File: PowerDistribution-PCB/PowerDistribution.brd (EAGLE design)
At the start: 166 x 53.5 mm, 47 parts, among them IC1 MAX3041CUE, IC2 MAX3041CUE, IC3 MAX3041CUE, IC4 MAX3041CUE, IC9 SN75176ASOIC

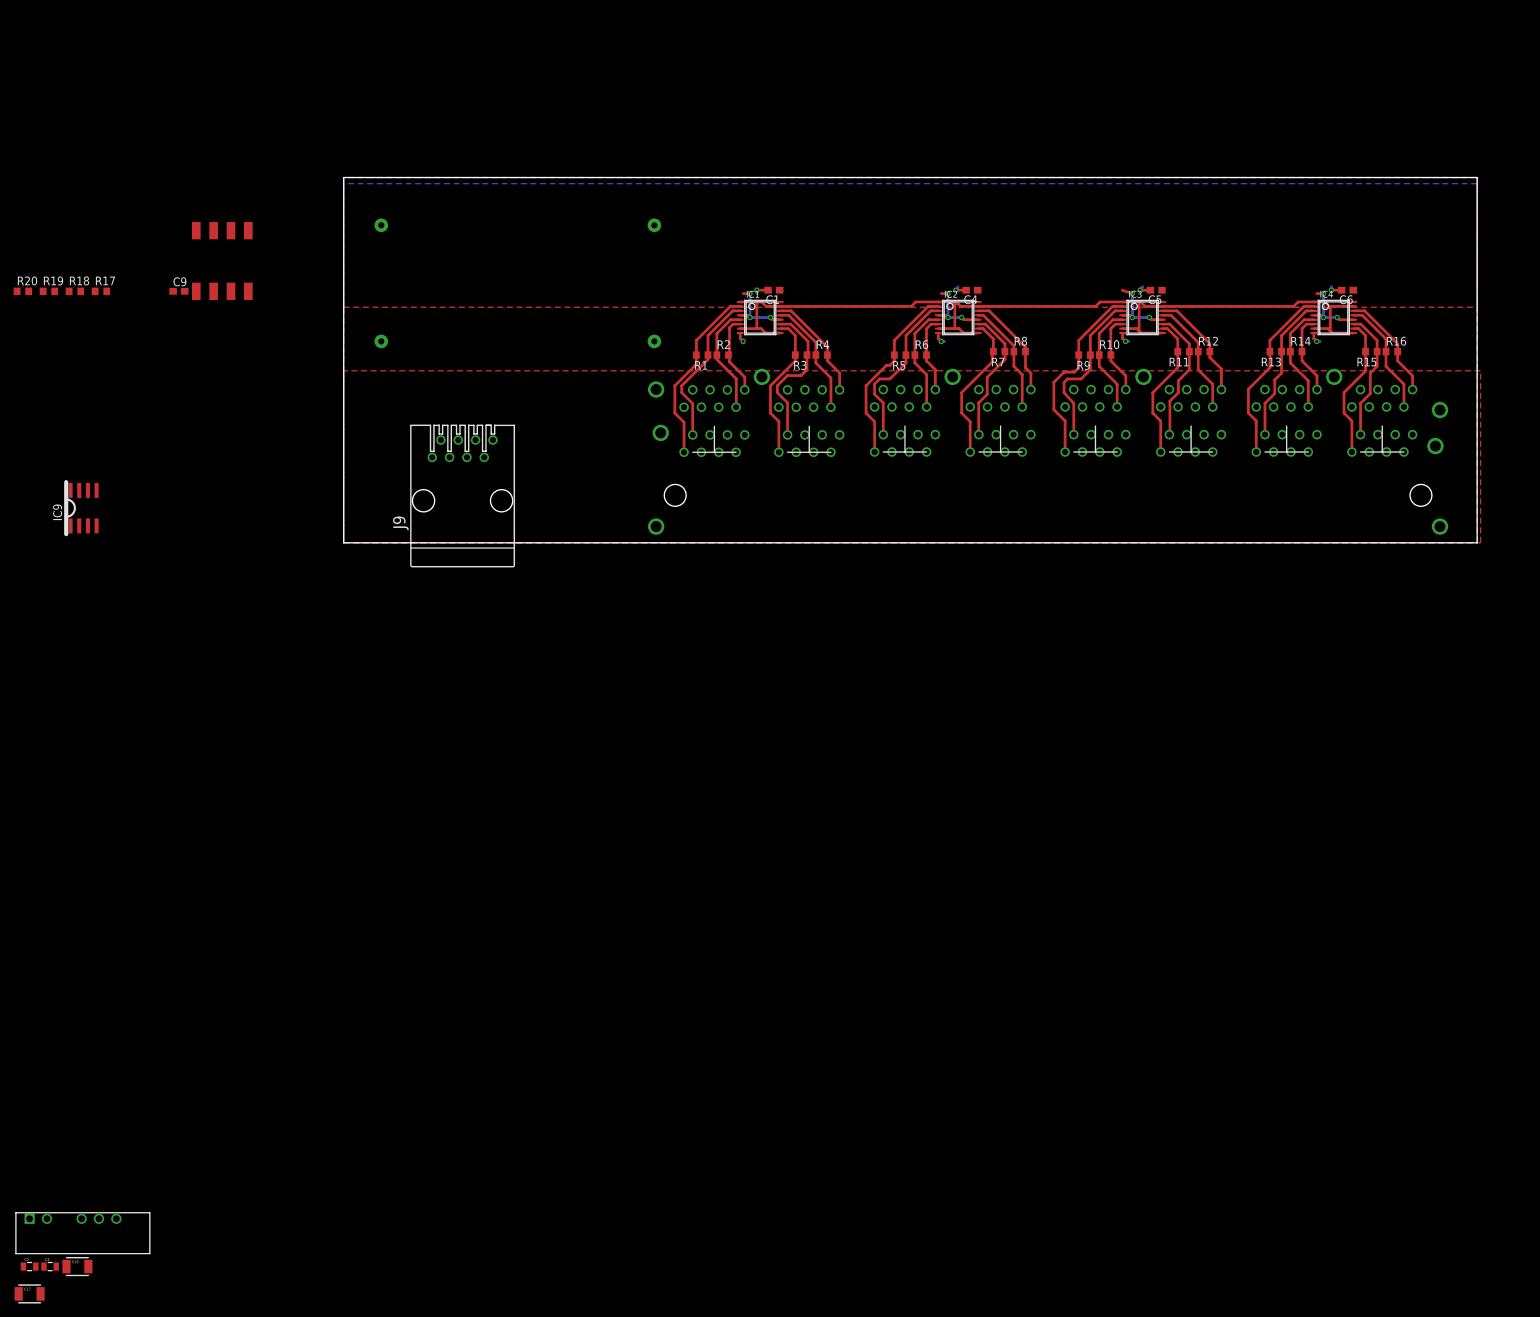
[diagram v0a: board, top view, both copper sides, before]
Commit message: Finish routing power distribution PCB; still need to fit to case
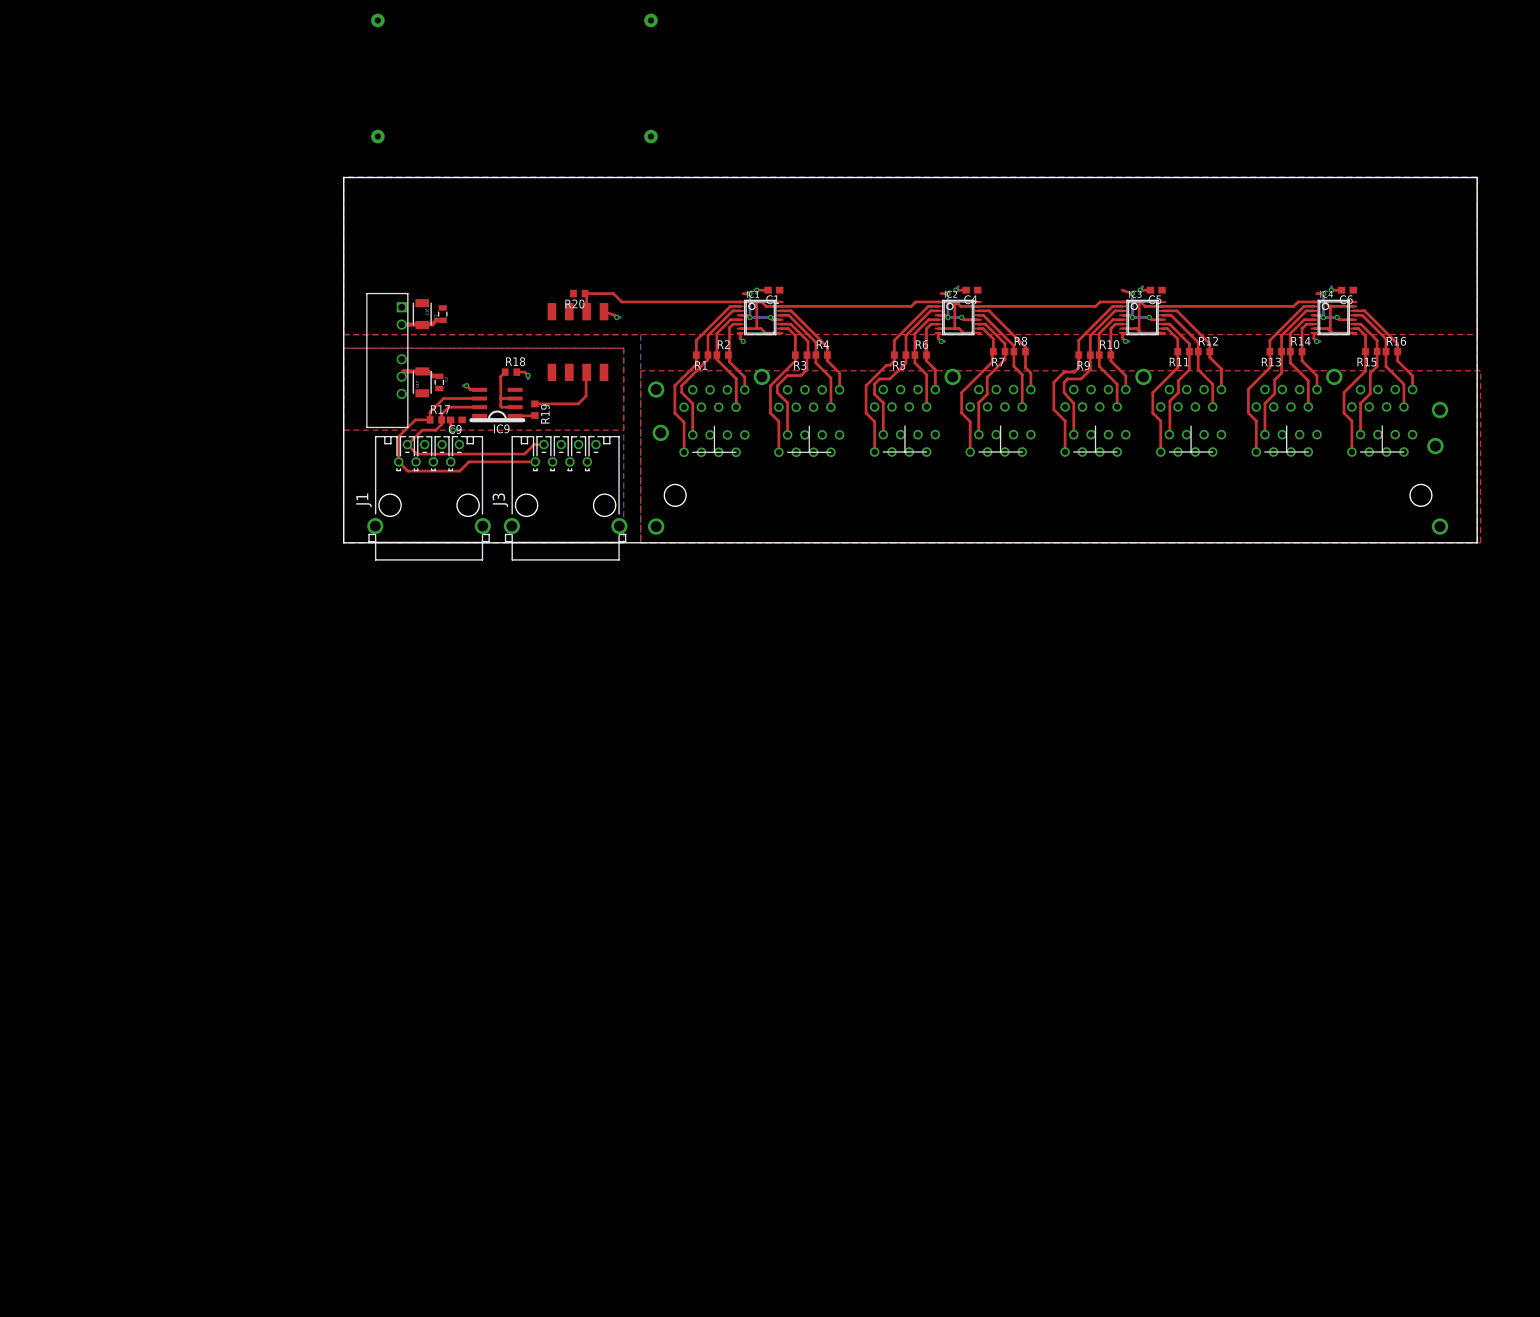
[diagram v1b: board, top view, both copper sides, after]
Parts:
- removed J9: (no value), con-amp:520426-4
- added J1, J3: (no value), con-amp:555153-1
- moved C2 152.1 mm to (14.5, 33.5), turned to 90 degrees
- moved C16 148.4 mm to (11.5, 33.5), turned to 270 degrees
- moved C17 145.4 mm to (11.5, 23.5), turned to 90 degrees
- moved U$10 144.2 mm to (8.50, 34.5), turned to 270 degrees
- moved C3 141.5 mm to (14.0, 23.5), turned to 270 degrees
- moved R20 81.5 mm to (34.5, 36.5), turned to 180 degrees
- moved R19 73.3 mm to (28.0, 19.5), turned to 270 degrees
- moved R18 65.0 mm to (24.5, 25.0)
- moved IC9 62.5 mm to (22.5, 20.5), turned to 90 degrees
- moved U$3 53.4 mm to (30.5, 27.5)
- moved R17 52.5 mm to (13.5, 18.0)
- moved C9 44.8 mm to (16.5, 18.0), turned to 180 degrees
- moved U$19 30.0 mm to (25.0, 68.0)
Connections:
- new net N$35: J1.3
- new net N$36: J1.4
- new net N$37: J1.5
- new net N$38: J1.6
- net GND_ISO: now also J1.7, J1.8, J3.7, J3.8; no longer J9.7, J9.8
- net RS485A9: now also J1.1, J3.1; no longer J9.1
- net RS485B9: now also J1.2, J3.2; no longer J9.2
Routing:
- net RS485A9: track 0.00 -> 39.7 mm
- net RS485B9: track 0.00 -> 34.9 mm
- net TX: track 131.5 -> 157.5 mm
- net GND_ISO: track 0.00 -> 14.0 mm, vias 0 -> 3
- net N$1: track 0.00 -> 11.5 mm
- net D9: track 0.00 -> 9.53 mm
- net GND: track 15.5 -> 24.4 mm, vias 8 -> 9
- net N$3: track 0.00 -> 2.90 mm
- added copper zone on layer 1, net 5V_ISO
- added copper zone on layer 16, net GND_ISO

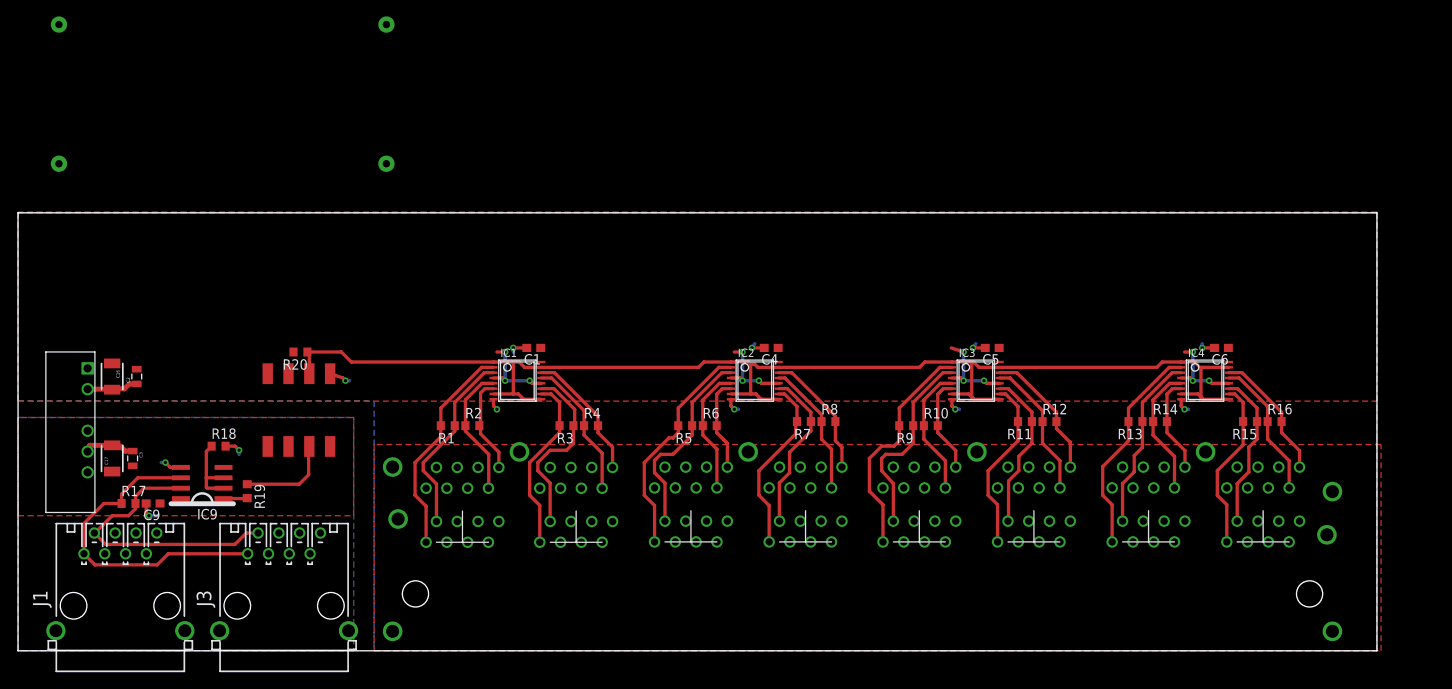
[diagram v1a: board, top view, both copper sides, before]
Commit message: Power Distribution: Finish layout, add mouting holes at edges (likely not quite enough), release RevA
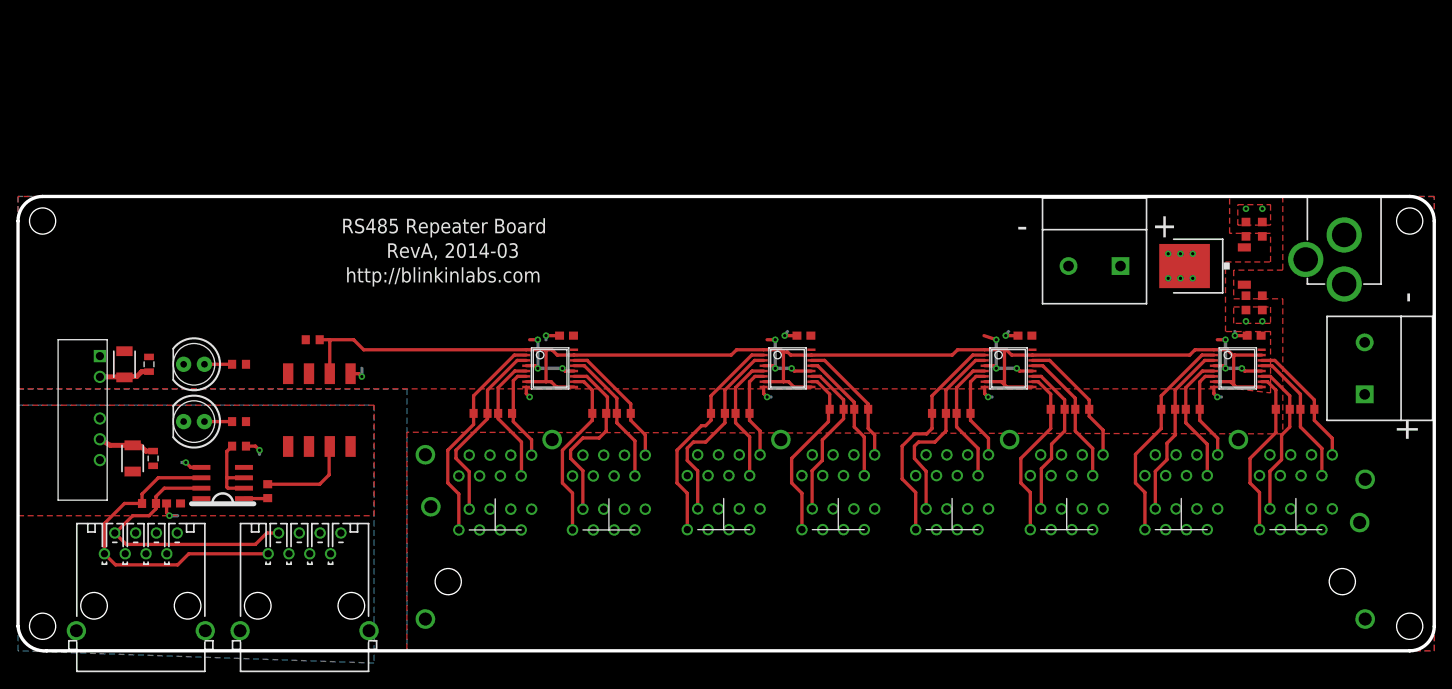
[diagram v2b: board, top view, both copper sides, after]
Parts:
- removed U$19: DC_DC, blinkinlabs:DSN2596
- added C11, C13: .3uF, adafruit:C0603K
- added C12, C14: 100nF, adafruit:C0603K
- added IC5: 7805DT, linear:TO252
- added J2: POWER_JACKPTH, SparkFun:POWER_JACK_PTH
- added JP1, JP13: (no value), SparkFun:SCREWTERMINAL-6.35MM-2
- added LED1, LED2: (no value), SparkFun:LED5MM
- added R21, R22: 1k, adafruit:R0603
- moved C1 4.27 mm to (67.0, 38.5)
- moved C4 4.27 mm to (96.0, 38.5)
- moved C5 4.27 mm to (123.0, 38.5)
- moved C6 4.27 mm to (151.0, 38.5)
- moved IC1 4.27 mm to (65.0, 34.5)
- moved IC2 4.27 mm to (94.0, 34.5)
- moved IC3 4.27 mm to (121.0, 34.5)
- moved IC4 4.27 mm to (149.0, 34.5)
- moved R1 4.27 mm to (56.5, 29.0)
- moved R10 4.27 mm to (115.5, 29.0)
- moved R11 4.27 mm to (127.0, 29.5)
- moved R12 4.27 mm to (130.0, 29.5)
- moved R13 4.27 mm to (140.5, 29.5)
- moved R14 4.27 mm to (143.5, 29.5)
- moved R15 4.27 mm to (154.5, 29.5)
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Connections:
- new net N$39: LED1.A, R21.1
- new net N$40: LED2.A, R22.1
- net +5V: now also C12.1, C14.1, IC5.2, JP13.P$1, R21.2; no longer U$19.OUT+
- net 5V_ISO: now also R22.2
- net GND: now also C11.2, C12.2, C13.2, C14.2, IC5.3, J2.GND, J2.GNDBREAK, JP1.P$2, JP13.P$2, LED1.K; no longer U$19.IN-, U$19.OUT-
- net GND_ISO: now also LED2.K
- net VIN: now also C11.1, C13.1, IC5.1, J2.PWR, JP1.P$1; no longer U$19.IN+
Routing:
- net TX: track 157.5 -> 161.8 mm
- net N$40: track 0.00 -> 3.38 mm
- net N$39: track 0.00 -> 3.38 mm
- net GND: track 24.4 -> 26.2 mm, vias 9 -> 19
- net GND_ISO: track 14.0 -> 14.6 mm
- added copper zone on layer 1, net GND
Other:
- board size 166 x 53.5 mm -> 173 x 55.5 mm
- board text added: "+"
- board text added: "-"
- board text added: "RS485 Repeater Board"
- board text added: "RevA, 2014-03"
- board text added: "http://blinkinlabs.com"
